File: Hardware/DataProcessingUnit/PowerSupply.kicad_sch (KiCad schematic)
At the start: 5 parts, among them U2 LD1117S33TR

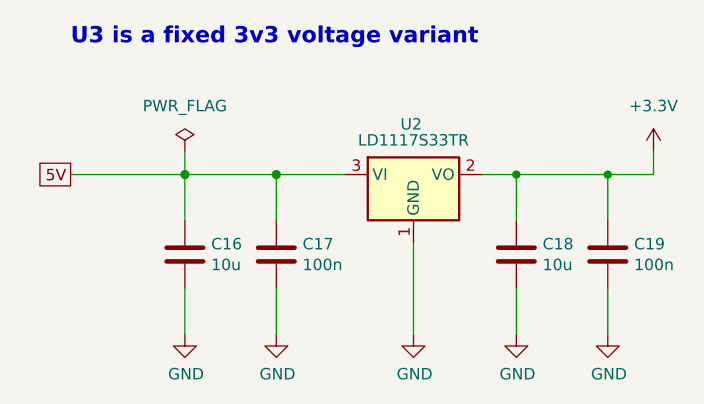
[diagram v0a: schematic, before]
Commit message: rework CI, make PCB smaller
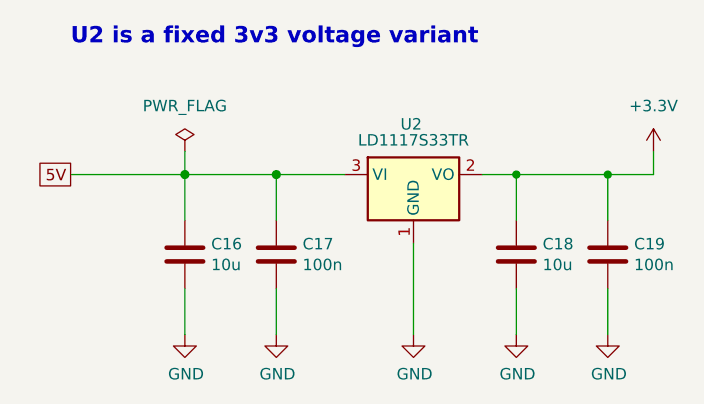
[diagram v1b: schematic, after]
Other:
- note added: "U2 is a fixed 3v3 voltage variant"
- note removed: "U3 is a fixed 3v3 voltage variant"
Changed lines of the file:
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@@
 	(generator_version "9.0")
 	(paper "A4")
-	(text "U3 is a fixed 3v3 voltage variant"
+	(text "U2 is a fixed 3v3 voltage variant"
 		(exclude_from_sim no)
 		(at 85.09 48.006 0)
